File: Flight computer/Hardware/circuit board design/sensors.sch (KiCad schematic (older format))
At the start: 5 parts, among them U10 BMI088, U8 MS5607-02BA

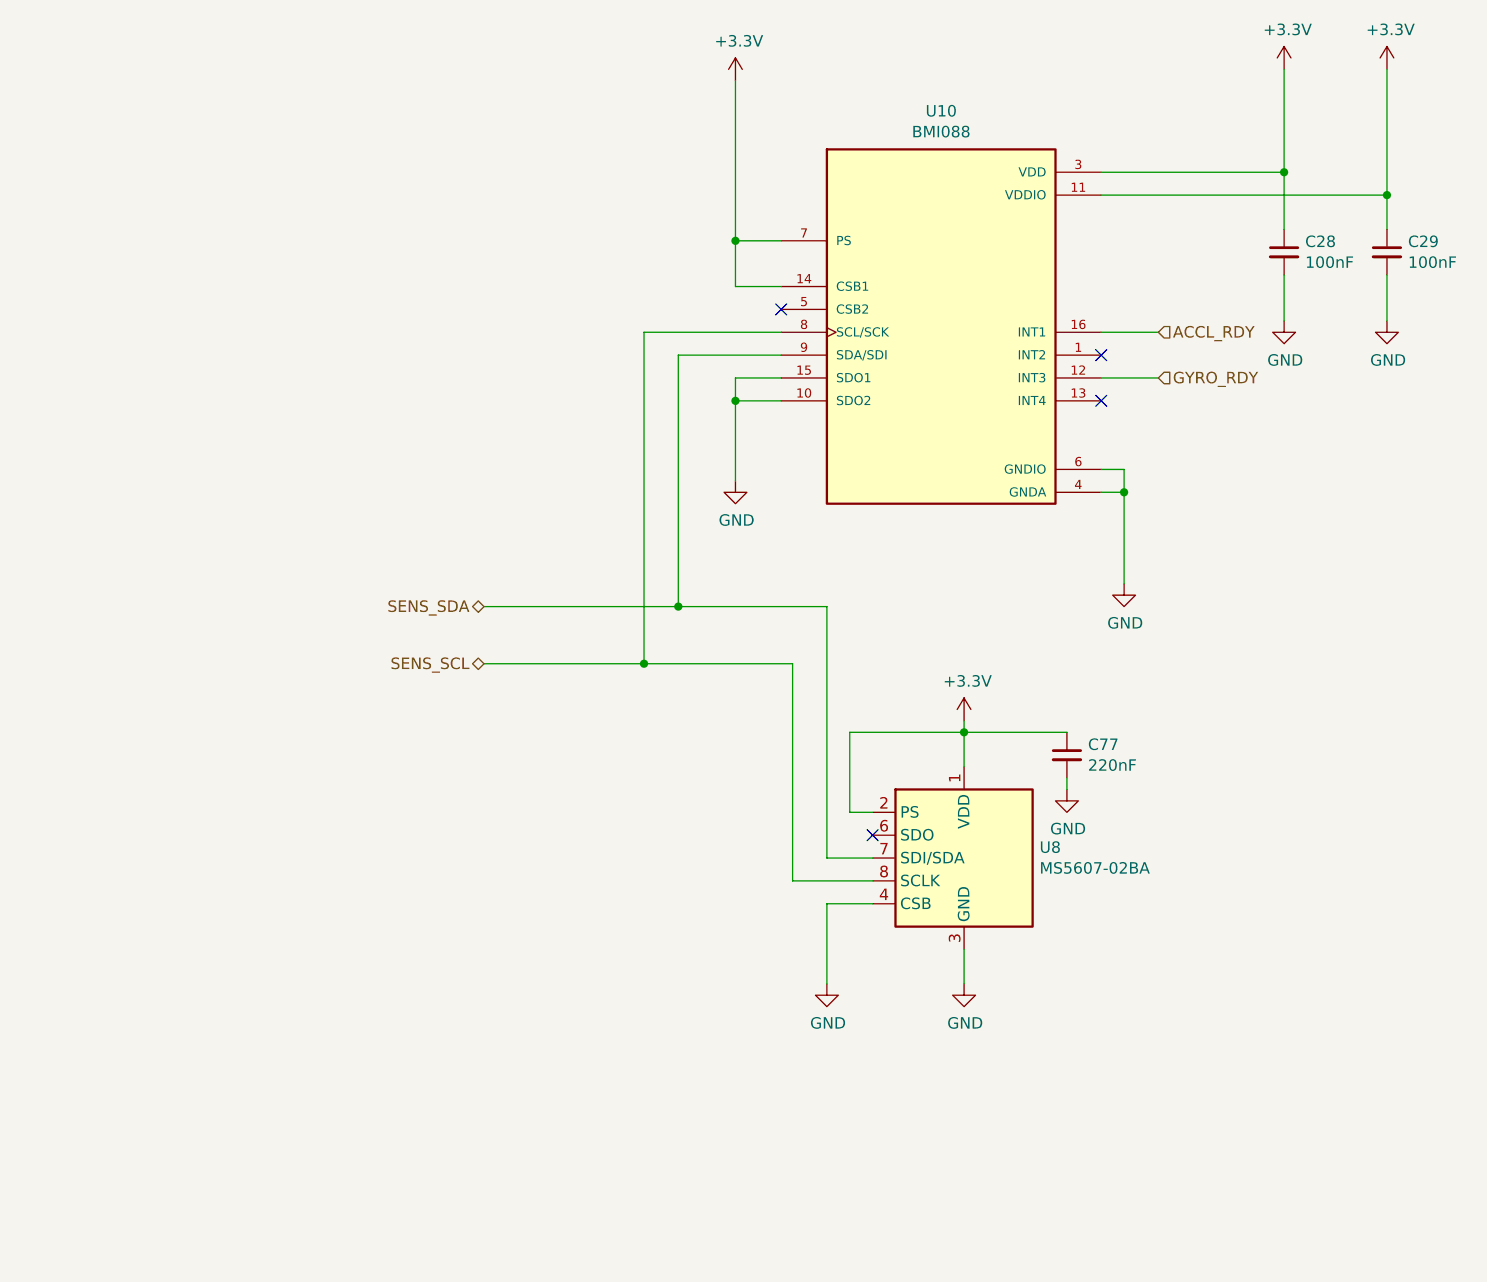
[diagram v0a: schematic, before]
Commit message: put in the IIS2MDC magnetometer
-fixed the error  spi connection pins for Flash chip
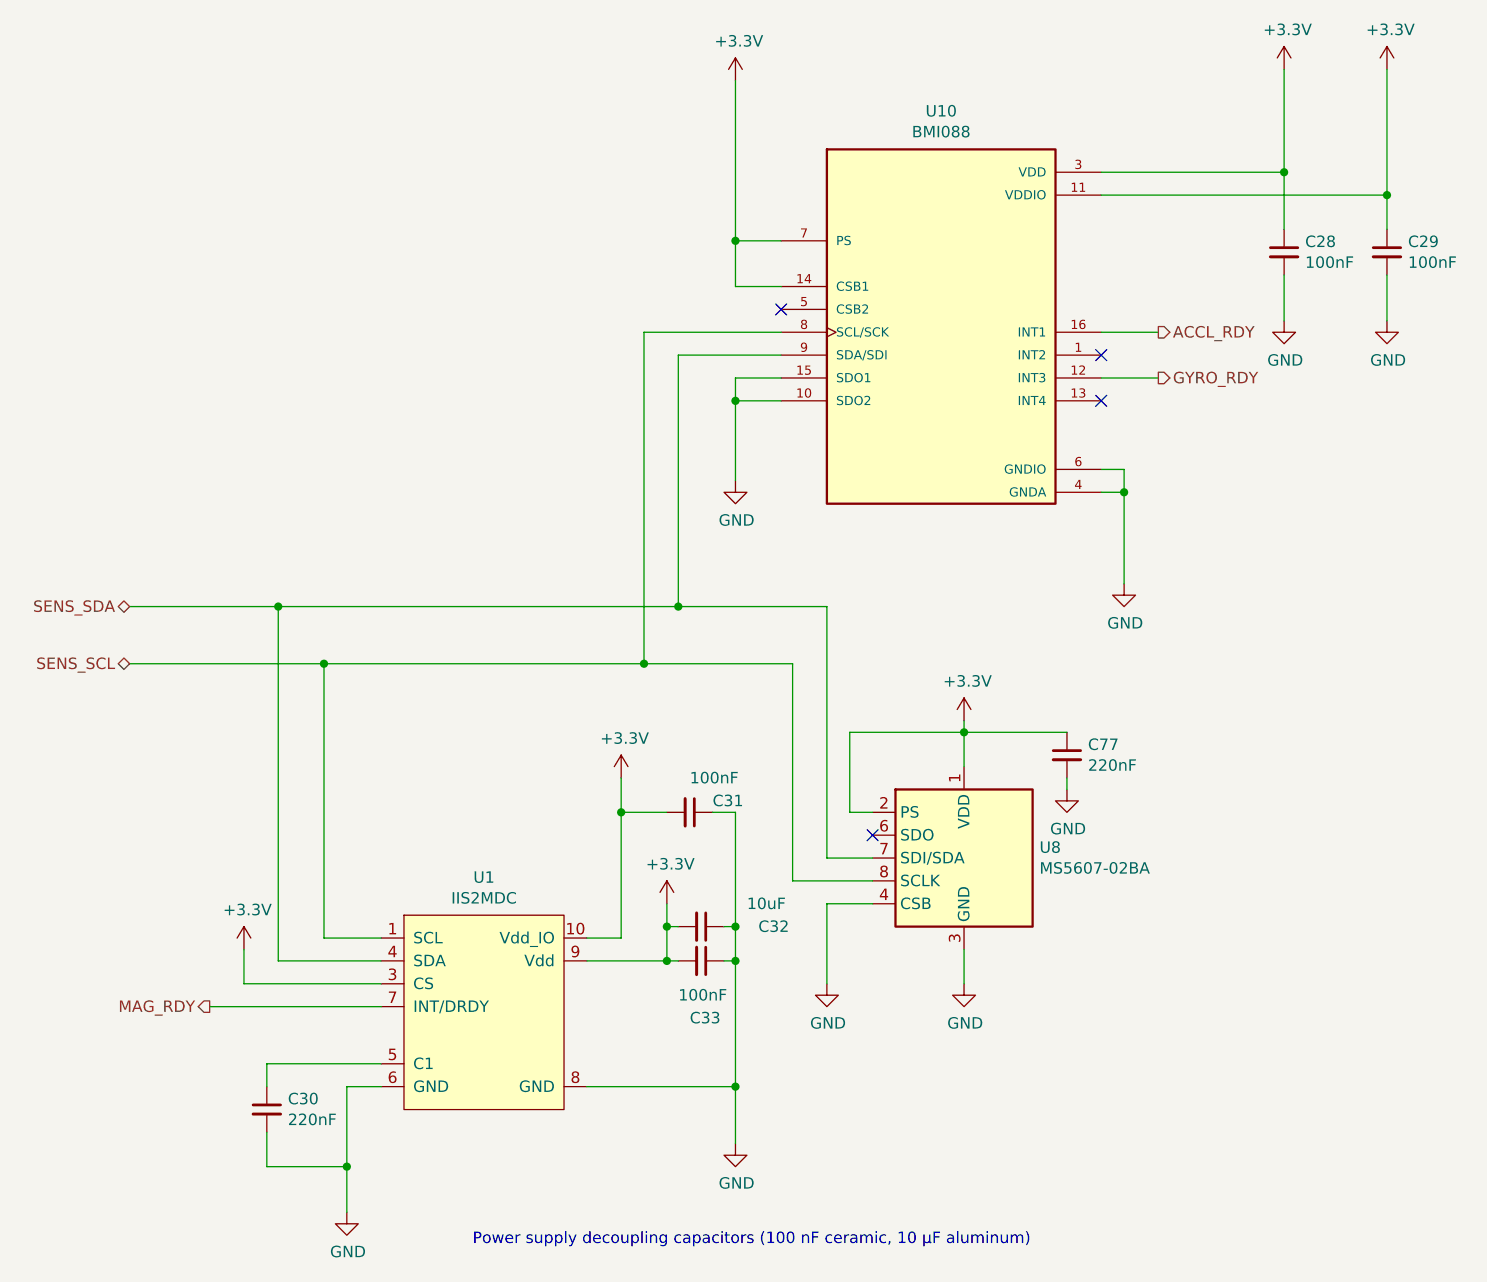
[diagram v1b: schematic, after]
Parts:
- added C30: 220nF, Capacitor_SMD:C_0402_1005Metric, symbol Device:C_Small
- added C31, C33: 100nF, Capacitor_SMD:C_0402_1005Metric, symbol Device:C_Small
- added C32: 10uF, Capacitor_SMD:C_0402_1005Metric, symbol Device:C_Small
- added U1: IIS2MDC, Package_LGA:LGA-12_2x2mm_P0.5mm, symbol flight-computer:IIS2MDC
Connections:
- net +3V3: now also C31.2, C32.2, C33.2, U1.10 (Vdd_IO), U1.3 (CS), U1.9 (Vdd)
- net GND: now also C30.2, C31.1, C32.1, C33.1, U1.6 (GND), U1.8 (GND)
- net SENS_SCL: now also U1.1 (SCL)
- net SENS_SDA: now also U1.4 (SDA)
- new net: C30.1, U1.5 (C1)
- new net MAG_RDY: U1.7 (INT/DRDY)
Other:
- note added: "Power supply decoupling capacitors (100 nF ceramic, 10 μF aluminum)"
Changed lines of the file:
@@
 	4450 4700 4950 4700
 NoConn ~ 4550 5150
-Text HLabel 2850 4150 0    50   BiDi ~ 0
-SENS_SDA
-Text HLabel 2850 4400 0    50   BiDi ~ 0
-SENS_SCL
 Wire Wire Line
 	5650 3550 5650 3650
@@
 	5550 3650 5650 3650
 Wire Wire Line
-	2850 4150 3700 4150
-Wire Wire Line
-	2850 4400 3550 4400
-Wire Wire Line
 	3550 2950 3550 4400
-Connection ~ 3550 4400
 Wire Wire Line
 	3550 4400 4200 4400
 Wire Wire Line
 	3700 3050 3700 4150
-Connection ~ 3700 4150
 Wire Wire Line
 	3700 4150 4350 4150
@@
 Wire Wire Line
 	6800 2350 6800 1800
-$Comp
-L power:+3.3V #PWR013
-U 1 1 5D6AE039
-P 4950 4650
-F 0 "#PWR013" H 4950 4500 50  0001 C CNN
-F 1 "+3.3V" H 4965 4823 50  0000 C CNN
-F 2 "" H 4950 4650 50  0001 C CNN
-F 3 "" H 4950 4650 50  0001 C CNN
-	1    4950 4650
-	1    0    0    -1
-$EndComp
 $Comp
 L power:+3.3V #PWR038
@@
 NoConn ~ 5550 3250
 NoConn ~ 5550 3050
-Text HLabel 5800 3150 2    50   Input ~ 0
+Text HLabel 5800 3150 2    50   Output ~ 0
 GYRO_RDY
-Text HLabel 5800 2950 2    50   Input ~ 0
+Text HLabel 5800 2950 2    50   Output ~ 0
 ACCL_RDY
 Wire Wire Line
@@
 	1    0    0    -1
 $EndComp
+Connection ~ 3700 4150
+Connection ~ 3550 4400
+Wire Wire Line
+	1300 4400 2150 4400
+Wire Wire Line
+	1300 4150 1950 4150
+Text HLabel 1300 4400 0    50   BiDi ~ 0
+SENS_SCL
+Text HLabel 1300 4150 0    50   BiDi ~ 0
+SENS_SDA
+Wire Wire Line
+	2250 6250 2400 6250
+$Comp
+L power:GND #PWR026
+U 1 1 5D8453A2
+P 2250 6800
+F 0 "#PWR026" H 2250 6550 50  0001 C CNN
+F 1 "GND" H 2255 6627 50  0000 C CNN
+F 2 "" H 2250 6800 50  0001 C CNN
+F 3 "" H 2250 6800 50  0001 C CNN
+	1    2250 6800
+	1    0    0    -1
+$EndComp
+Wire Wire Line
+	2400 5600 2150 5600
+Wire Wire Line
+	2150 5600 2150 4400
+Connection ~ 2150 4400
+Wire Wire Line
+	2150 4400 3550 4400
+Wire Wire Line
+	2400 5700 1950 5700
+Wire Wire Line
+	1950 5700 1950 4150
+Connection ~ 1950 4150
+Wire Wire Line
+	1950 4150 3700 4150
+Wire Wire Line
+	1900 6150 1900 6250
+Wire Wire Line
+	2400 6150 1900 6150
+$Comp
+L Device:C_Small C30
+U 1 1 5D8480A6
+P 1900 6350
+F 0 "C30" H 1992 6396 50  0000 L CNN
+F 1 "220nF" H 1992 6305 50  0000 L CNN
+F 2 "Capacitor_SMD:C_0402_1005Metric" H 1900 6350 50  0001 C CNN
+F 3 "~" H 1900 6350 50  0001 C CNN
+	1    1900 6350
+	1    0    0    -1
+$EndComp
+Wire Wire Line
+	2250 6250 2250 6600
+Wire Wire Line
+	1900 6450 1900 6600
+Wire Wire Line
+	1900 6600 2250 6600
+Connection ~ 2250 6600
+Wire Wire Line
+	2250 6600 2250 6800
+Wire Wire Line
+	3950 6250 3950 5700
+Wire Wire Line
+	3950 5050 3850 5050
+Wire Wire Line
+	3450 5050 3450 5600
+Wire Wire Line
+	3450 5600 3300 5600
+Wire Wire Line
+	3450 5050 3450 4900
+Connection ~ 3450 5050
+$Comp
+L power:+3.3V #PWR013
+U 1 1 5D6AE039
+P 4950 4650
+F 0 "#PWR013" H 4950 4500 50  0001 C CNN
+F 1 "+3.3V" H 4965 4823 50  0000 C CNN
+F 2 "" H 4950 4650 50  0001 C CNN
+F 3 "" H 4950 4650 50  0001 C CNN
+	1    4950 4650
+	1    0    0    -1
+$EndComp
+$Comp
+L power:+3.3V #PWR027
+U 1 1 5D8636CD
+P 3450 4900
+F 0 "#PWR027" H 3450 4750 50  0001 C CNN
+F 1 "+3.3V" H 3465 5073 50  0000 C CNN
+F 2 "" H 3450 4900 50  0001 C CNN
+F 3 "" H 3450 4900 50  0001 C CNN
+	1    3450 4900
+	1    0    0    -1
+$EndComp
+$Comp
+L Device:C_Small C31
+U 1 1 5D863BFF
+P 3750 5050
+F 0 "C31" V 3700 5150 50  0000 L CNN
+F 1 "100nF" V 3600 5050 50  0000 L CNN
+F 2 "Capacitor_SMD:C_0402_1005Metric" H 3750 5050 50  0001 C CNN
+F 3 "~" H 3750 5050 50  0001 C CNN
+	1    3750 5050
+	0    1    1    0
+$EndComp
+Wire Wire Line
+	3650 5050 3450 5050
+Wire Wire Line
+	3950 6250 3950 6500
+$Comp
+L power:GND #PWR046
+U 1 1 5D833856
+P 3950 6500
+F 0 "#PWR046" H 3950 6250 50  0001 C CNN
+F 1 "GND" H 3955 6327 50  0000 C CNN
+F 2 "" H 3950 6500 50  0001 C CNN
+F 3 "" H 3950 6500 50  0001 C CNN
+	1    3950 6500
+	1    0    0    -1
+$EndComp
+Connection ~ 3950 6250
+Wire Wire Line
+	3300 6250 3950 6250
+Wire Wire Line
+	3300 5700 3650 5700
+Connection ~ 3950 5700
+Wire Wire Line
+	3950 5700 3950 5550
+Wire Wire Line
+	3650 5550 3650 5700
+Connection ~ 3650 5700
+Wire Wire Line
+	3650 5700 3700 5700
+Wire Wire Line
+	3650 5550 3700 5550
+Connection ~ 3950 5550
+Wire Wire Line
+	3950 5550 3950 5050
+Wire Wire Line
+	3650 5550 3650 5450
+Connection ~ 3650 5550
+$Comp
+L power:+3.3V #PWR047
+U 1 1 5D86DF75
+P 3650 5450
+F 0 "#PWR047" H 3650 5300 50  0001 C CNN
+F 1 "+3.3V" H 3665 5623 50  0000 C CNN
+F 2 "" H 3650 5450 50  0001 C CNN
+F 3 "" H 3650 5450 50  0001 C CNN
+	1    3650 5450
+	1    0    0    -1
+$EndComp
+$Comp
+L Device:C_Small C32
+U 1 1 5D86E3A8
+P 3800 5550
+F 0 "C32" V 3800 5800 50  0000 L CNN
+F 1 "10uF" V 3700 5750 50  0000 L CNN
+F 2 "Capacitor_SMD:C_0402_1005Metric" H 3800 5550 50  0001 C CNN
+F 3 "~" H 3800 5550 50  0001 C CNN
+	1    3800 5550
+	0    1    1    0
+$EndComp
+Wire Wire Line
+	3900 5550 3950 5550
+$Comp
+L Device:C_Small C33
+U 1 1 5D86E64A
+P 3800 5700
+F 0 "C33" V 4050 5650 50  0000 L CNN
+F 1 "100nF" V 3950 5600 50  0000 L CNN
+F 2 "Capacitor_SMD:C_0402_1005Metric" H 3800 5700 50  0001 C CNN
+F 3 "~" H 3800 5700 50  0001 C CNN
+	1    3800 5700
+	0    1    1    0
+$EndComp
+Wire Wire Line
+	3900 5700 3950 5700
+Text Notes 2800 6950 0    50   ~ 0
+Power supply decoupling capacitors (100 nF ceramic, 10 μF aluminum)
+$Comp
+L flight-computer:IIS2MDC U1
+U 1 1 5D82B1DE
+P 2850 5600
+F 0 "U1" H 2850 5865 50  0000 C CNN
+F 1 "IIS2MDC" H 2850 5774 50  0000 C CNN
+F 2 "Package_LGA:LGA-12_2x2mm_P0.5mm" H 2850 5600 50  0001 C CNN
+F 3 "https://www.mouser.co.uk/datasheet/2/389/iis2mdc-1309412.pdf" H 2850 5600 50  0001 C CNN
+F 4 "https://www.mouser.co.uk/ProductDetail/STMicroelectronics/IIS2MDCTR?qs=sGAEpiMZZMve4%2FbfQkoj%252BNsA%2FYLrKsWenI%252BNJIvEAfE%3D" H 2850 5600 50  0001 C CNN "Purchase link"
+F 5 "1.93" H 2850 5600 50  0001 C CNN "Cost"
+	1    2850 5600
+	1    0    0    -1
+$EndComp
+Wire Wire Line
+	2400 5800 1800 5800
+Wire Wire Line
+	1800 5800 1800 5650
+$Comp
+L power:+3.3V #PWR0105
+U 1 1 5D87344D
+P 1800 5650
+F 0 "#PWR0105" H 1800 5500 50  0001 C CNN
+F 1 "+3.3V" H 1815 5823 50  0000 C CNN
+F 2 "" H 1800 5650 50  0001 C CNN
+F 3 "" H 1800 5650 50  0001 C CNN
+	1    1800 5650
+	1    0    0    -1
+$EndComp
+Text HLabel 1650 5900 0    50   Output ~ 0
+MAG_RDY
+Wire Wire Line
+	1650 5900 2400 5900
 $EndSCHEMATC

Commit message: Wired up the FETs
-fixed the ERC error for the BMI088 symbol
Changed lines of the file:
@@
 	1    0    0    -1
 $EndComp
-Wire Wire Line
-	4150 3150 3950 3150
 $Comp
 L power:GND #PWR014
@@
 Wire Wire Line
 	1650 5900 2400 5900
+Wire Wire Line
+	3950 3150 4150 3150
 $EndSCHEMATC

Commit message: added in the footprint for the 6 terminal block
routed the RF section with the 434 antenna
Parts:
- C28, C29, C30, C31, C32, C33, C77: footprint Capacitor_SMD:C_0402_1005Metric -> Capacitor_SMD:C_0603_1608Metric
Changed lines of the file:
@@
 F 0 "C33" V 4050 5650 50  0000 L CNN
 F 1 "100nF" V 3950 5600 50  0000 L CNN
-F 2 "Capacitor_SMD:C_0402_1005Metric" H 3800 5700 50  0001 C CNN
+F 2 "Capacitor_SMD:C_0603_1608Metric" H 3800 5700 50  0001 C CNN
 F 3 "~" H 3800 5700 50  0001 C CNN
 	1    3800 5700
@@
 F 0 "C32" V 3800 5800 50  0000 L CNN
 F 1 "10uF" V 3700 5750 50  0000 L CNN
-F 2 "Capacitor_SMD:C_0402_1005Metric" H 3800 5550 50  0001 C CNN
+F 2 "Capacitor_SMD:C_0603_1608Metric" H 3800 5550 50  0001 C CNN
 F 3 "~" H 3800 5550 50  0001 C CNN
 	1    3800 5550
@@
 F 0 "C31" V 3700 5150 50  0000 L CNN
 F 1 "100nF" V 3600 5050 50  0000 L CNN
-F 2 "Capacitor_SMD:C_0402_1005Metric" H 3750 5050 50  0001 C CNN
+F 2 "Capacitor_SMD:C_0603_1608Metric" H 3750 5050 50  0001 C CNN
 F 3 "~" H 3750 5050 50  0001 C CNN
 	1    3750 5050
@@
 F 0 "C30" H 1992 6396 50  0000 L CNN
 F 1 "220nF" H 1992 6305 50  0000 L CNN
-F 2 "Capacitor_SMD:C_0402_1005Metric" H 1900 6350 50  0001 C CNN
+F 2 "Capacitor_SMD:C_0603_1608Metric" H 1900 6350 50  0001 C CNN
 F 3 "~" H 1900 6350 50  0001 C CNN
 	1    1900 6350
@@
 F 0 "C29" H 6892 2646 50  0000 L CNN
 F 1 "100nF" H 6892 2555 50  0000 L CNN
-F 2 "Capacitor_SMD:C_0402_1005Metric" H 6800 2600 50  0001 C CNN
+F 2 "Capacitor_SMD:C_0603_1608Metric" H 6800 2600 50  0001 C CNN
 F 3 "~" H 6800 2600 50  0001 C CNN
 	1    6800 2600
@@
 F 0 "C28" H 6442 2646 50  0000 L CNN
 F 1 "100nF" H 6442 2555 50  0000 L CNN
-F 2 "Capacitor_SMD:C_0402_1005Metric" H 6350 2600 50  0001 C CNN
+F 2 "Capacitor_SMD:C_0603_1608Metric" H 6350 2600 50  0001 C CNN
 F 3 "~" H 6350 2600 50  0001 C CNN
 	1    6350 2600
@@
 F 0 "C77" H 5492 4846 50  0000 L CNN
 F 1 "220nF" H 5492 4755 50  0000 L CNN
-F 2 "Capacitor_SMD:C_0402_1005Metric" H 5400 4800 50  0001 C CNN
+F 2 "Capacitor_SMD:C_0603_1608Metric" H 5400 4800 50  0001 C CNN
 F 3 "~" H 5400 4800 50  0001 C CNN
 	1    5400 4800

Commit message: updated links to purchasing several components
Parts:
- U8: Cost (none) -> 2.42
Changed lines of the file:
@@
 F 3 "https://www.te.com/commerce/DocumentDelivery/DDEController?Action=showdoc&DocId=Data+Sheet%7FMS5607-02BA03%7FB2%7Fpdf%7FEnglish%7FENG_DS_MS5607-02BA03_B2.pdf%7FCAT-BLPS0035" H 4950 5250 50  0001 C CNN
 F 4 "https://www.mouser.co.uk/ProductDetail/Measurement-Specialties/MS560702BA03-50?qs=sGAEpiMZZMvhQj7WZhFIANHEKf5NWCaHepyHiZrEptc%3D" H 4950 5250 50  0001 C CNN "Purchase link"
+F 5 "2.42" H 4950 5250 50  0001 C CNN "Cost"
 	1    4950 5250
 	1    0    0    -1
